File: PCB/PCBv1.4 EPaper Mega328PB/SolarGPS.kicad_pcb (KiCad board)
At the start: 2 copper layers, 80 x 32 mm, 53 parts, among them J1 Conn_01x24_Female, J2 GND, J3 GND, J4 AVR-ISP-6, J5 Solar2+, J6 Solar1+, J7 Screw_Terminal_01x01, J8 Conn_01x04_Male, Q1 Q_NMOS_GSD, U1 TPS63802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

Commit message: add tqfp footprint
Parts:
- added U4: ATmega328PB-A, Package_QFP:TQFP-32_7x7mm_P0.8mm, B.Cu at (85.3, 74.8)
- moved C10 3.82 mm to (76.0, 81.2), turned to 180 degrees
- moved C17 2.83 mm to (83.3, 67.9)
- moved U3 2.34 mm to (85.3, 74.9)
- moved C19 2.26 mm to (85.7, 68.6)
- moved C18 2.00 mm to (64.6, 78.7)
- moved J4 2.00 mm to (71.9, 77.9)
- moved C26 1.55 mm to (78.2, 70.3)
- moved U6 1.52 mm to (75.5, 70.9)
- moved C14 1.50 mm to (84.7, 81.0), turned to 180 degrees
- moved C4 1.06 mm to (76.0, 79.6), turned to 180 degrees
- moved Y1 0.07 mm to (78.7, 79.9), turned to -90 degrees
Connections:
- net Net-(C19-Pad1) renamed AREF
- C10 pad 1: Net-(C10-Pad1) -> XTAL1
- C4 pad 1: Net-(C4-Pad1) -> XTAL2
- U3 pad 7: Net-(C4-Pad1) -> XTAL1
- U3 pad 8: Net-(C10-Pad1) -> XTAL2
- Y1 pad 1: Net-(C10-Pad1) -> XTAL1
- Y1 pad 2: Net-(C4-Pad1) -> XTAL2
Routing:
- net XTAL1: track 0.00 -> 10.1 mm
- net XTAL2: track 0.00 -> 8.53 mm
- net GND: track 12.1 -> 20.5 mm, vias 79 -> 81
- net RESET: track 29.2 -> 36.8 mm
- net Net-(C4-Pad1): track 6.96 -> 0.00 mm
- net Net-(C10-Pad1): track 5.06 -> 0.00 mm
- net LIS_CS: track 12.7 -> 17.3 mm
- net VDD: track 160.7 -> 165.2 mm, vias 4 -> 5
- net SPI_MISO: track 16.9 -> 20.9 mm
- net DISP_CS: track 26.0 -> 30.0 mm
- net SPI_CLK: track 31.2 -> 34.5 mm
- net LED: track 23.3 -> 26.3 mm, vias 2 -> 0
- net DISP_DC: track 27.0 -> 30.0 mm
- net DISP_RES#: track 28.2 -> 30.5 mm
- net GPS_UART_MOSI: track 47.7 -> 45.5 mm
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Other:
- board text removed: "APPLY DIRECTLY TO EYEBALLS"

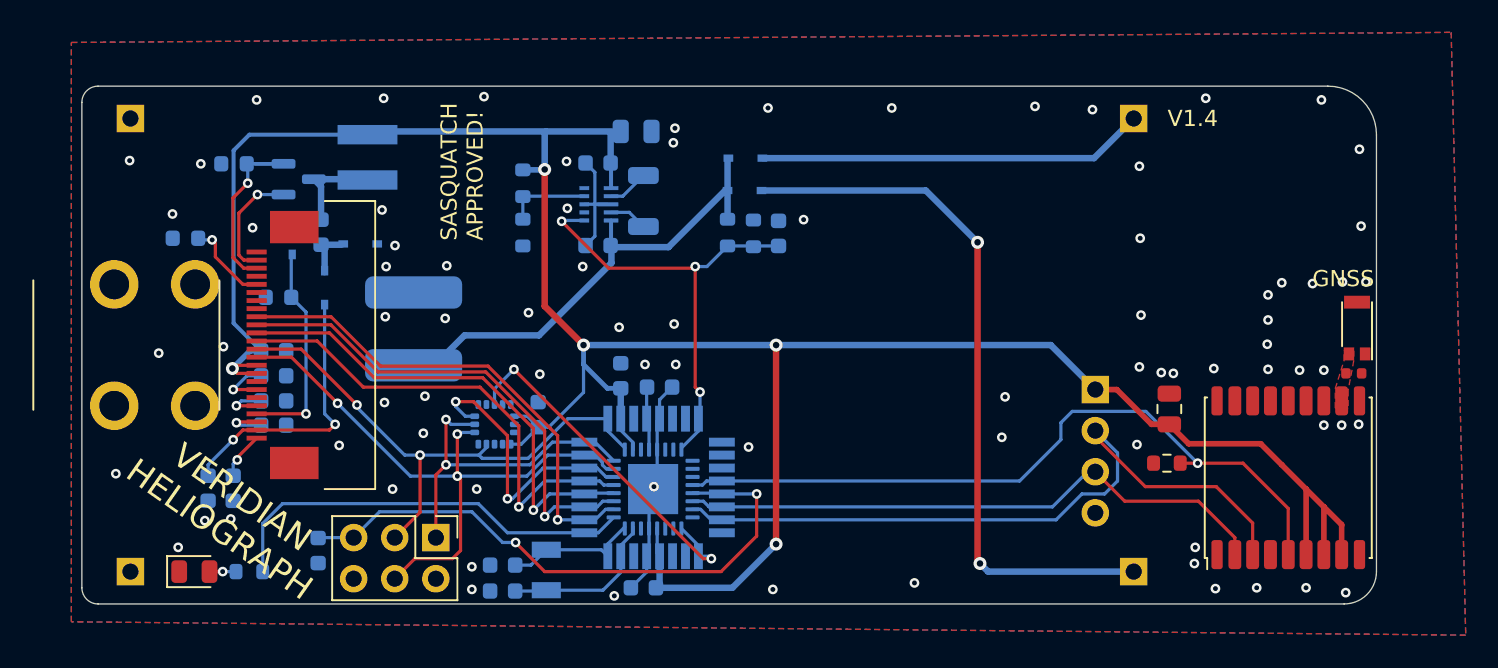
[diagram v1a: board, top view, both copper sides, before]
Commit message: reduce power BOM
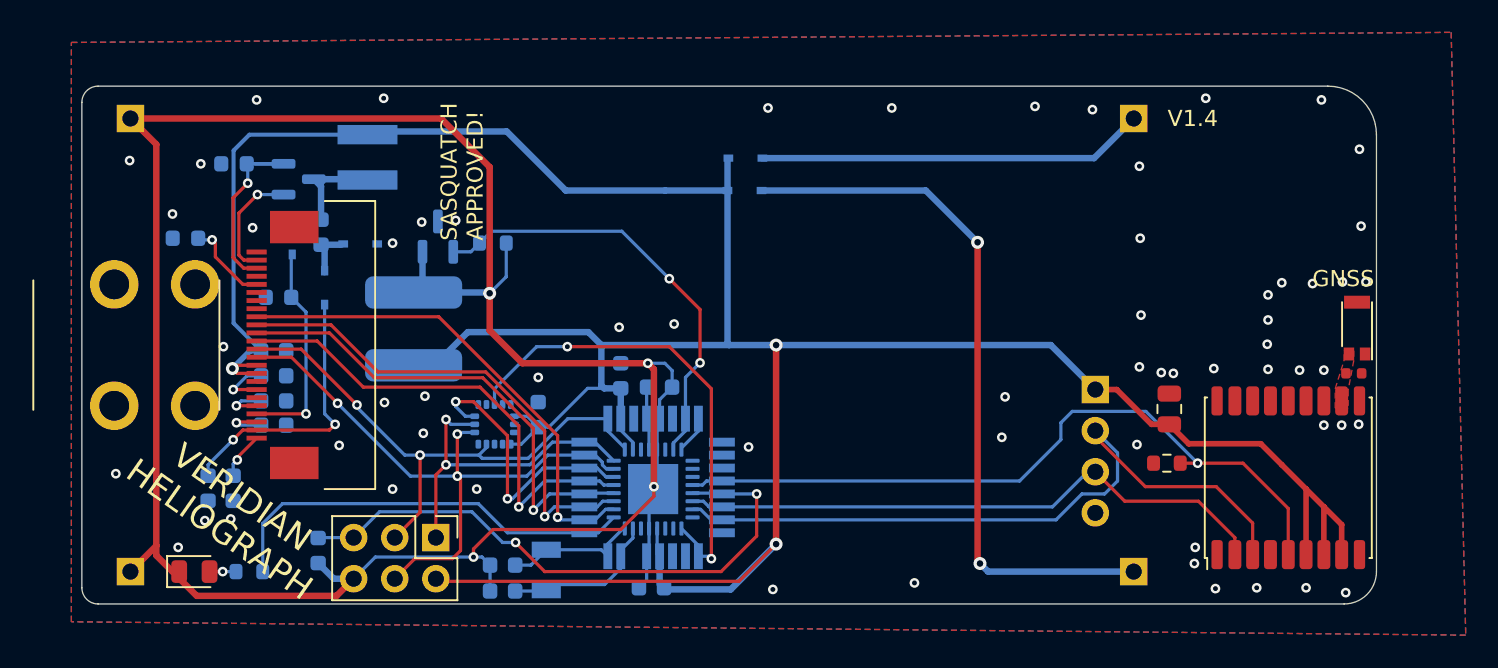
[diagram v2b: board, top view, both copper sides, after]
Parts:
- removed C11: 10nF, Capacitor_SMD:C_0603_1608Metric
- removed C12: 47uF, Capacitor_SMD:C_0805_2012Metric
- removed C13, C7: 1uF, Capacitor_SMD:C_0603_1608Metric
- removed L2: 0.47uH, Inductor_SMD:L_1206_3216Metric
- removed R12, R13: 1M, Resistor_SMD:R_0603_1608Metric
- removed R4: 91k, Resistor_SMD:R_0603_1608Metric
- removed U1: TPS63802, Margo_Lib:VREG_TPS63802DLAR
- added Q2: Q_NMOS_GSD, Package_TO_SOT_SMD:SOT-23, B.Cu at (72.0, 59.3)
- R1: value 432k -> 1M
- moved R1 4.14 mm to (75.4, 59.7), turned to 180 degrees
- moved C14 0.50 mm to (85.2, 81.0)
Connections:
- C10 pad 2: GND -> GNDPWR
- C14 pad 1: VDD -> VBAT
- C14 pad 2: GND -> GNDPWR
- C15 pad 2: VDD -> VBAT
- C17 pad 1: VDD -> VBAT
- C17 pad 2: GND -> GNDPWR
- C18 pad 1: GND -> GNDPWR
- C19 pad 2: GND -> GNDPWR
- C26 pad 2: VDD -> VBAT
- C4 pad 2: GND -> GNDPWR
- C5 pad 1: VDD -> VBAT
- C8 pad 2: GND -> GNDPWR
- D2 pad 1: GND -> GNDPWR
- J1 pad 15: VDD -> VBAT
- J1 pad 16: VDD -> VBAT
- J2 pad 1: GND -> GNDPWR
- J3 pad 1: GND -> GNDPWR
- J4 pad 2: VDD -> VBAT
- J4 pad 6: GND -> GNDPWR
- J8 pad 1: VDD -> VBAT
- L1 pad 1: VDD -> VBAT
- R1 pad 1: Net-(R1-Pad1) -> GNDPWR
- R1 pad 2: VDD -> ACCSW
- U2 pad 6: VDD -> VBAT
- U2 pad 7: VDD -> VBAT
- U2 pad 8: VDD -> VBAT
- U3 pad 18: VDD -> VBAT
- U3 pad 21: GND -> GNDPWR
- U3 pad 23: unconnected-(U3-Pad23) -> ACCSW
- U3 pad 33: GND -> GNDPWR
- U3 pad 4: VDD -> VBAT
- U3 pad 5: GND -> GNDPWR
- U4 pad 18: VDD -> VBAT
- U4 pad 21: GND -> GNDPWR
- U4 pad 23: unconnected-(U4-Pad23) -> ACCSW
- U4 pad 4: VDD -> VBAT
- U4 pad 5: GND -> GNDPWR
- U6 pad 1: VDD -> VBAT
- U6 pad 14: VDD -> VBAT
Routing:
- net VBAT: track 30.9 -> 199.5 mm, vias 0 -> 3
- net VDD: track 165.2 -> 0.00 mm, vias 5 -> 0
- net GNDPWR: track 0.00 -> 151.4 mm, vias 0 -> 4
- net ACCSW: track 0.00 -> 27.1 mm, vias 0 -> 2
- net VBAT_SENSE: track 28.4 -> 2.25 mm, vias 3 -> 0
- net GND: track 20.5 -> 0.00 mm, vias 81 -> 63
- net LIS_INT: track 22.7 -> 30.0 mm
- net Net-(R1-Pad1): track 5.21 -> 0.00 mm
- net Net-(L2-Pad2): track 2.53 -> 0.00 mm
- net Net-(L2-Pad1): track 2.36 -> 0.00 mm
